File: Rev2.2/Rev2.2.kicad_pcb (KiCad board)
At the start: 4 copper layers, 91.8 x 94.5 mm, 120 parts, among them J1 Termination, J10 USART1, J11 3.3V power breakout, J12 5V power breakout, J13 AIN1, J14 USB C PWR, J15 USART6, J16 AIN2, J17 AIN3, J18 AIN4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

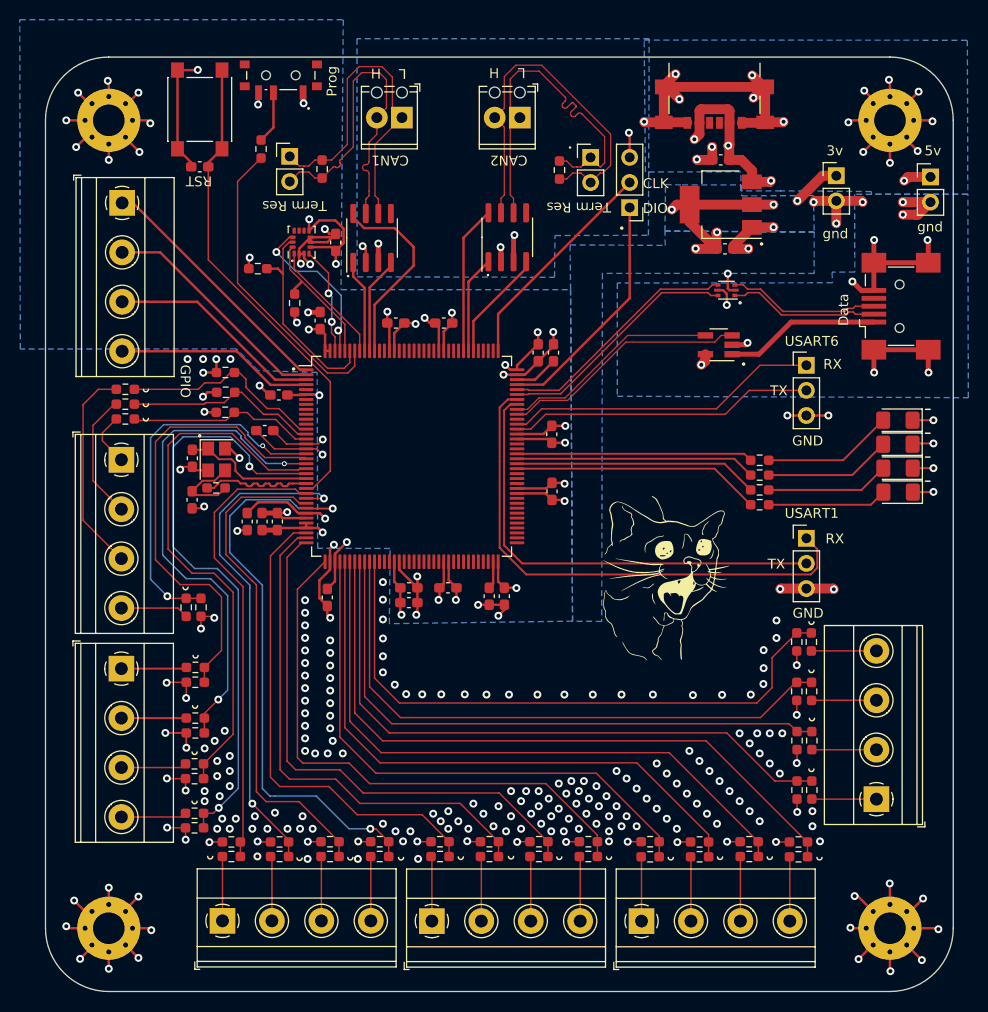
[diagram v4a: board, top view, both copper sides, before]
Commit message: added labels that tell you which pins the connectors are connected to for analog, GPIO, and LEDs. Also added a label for the USB C connector called Power to indicate its function
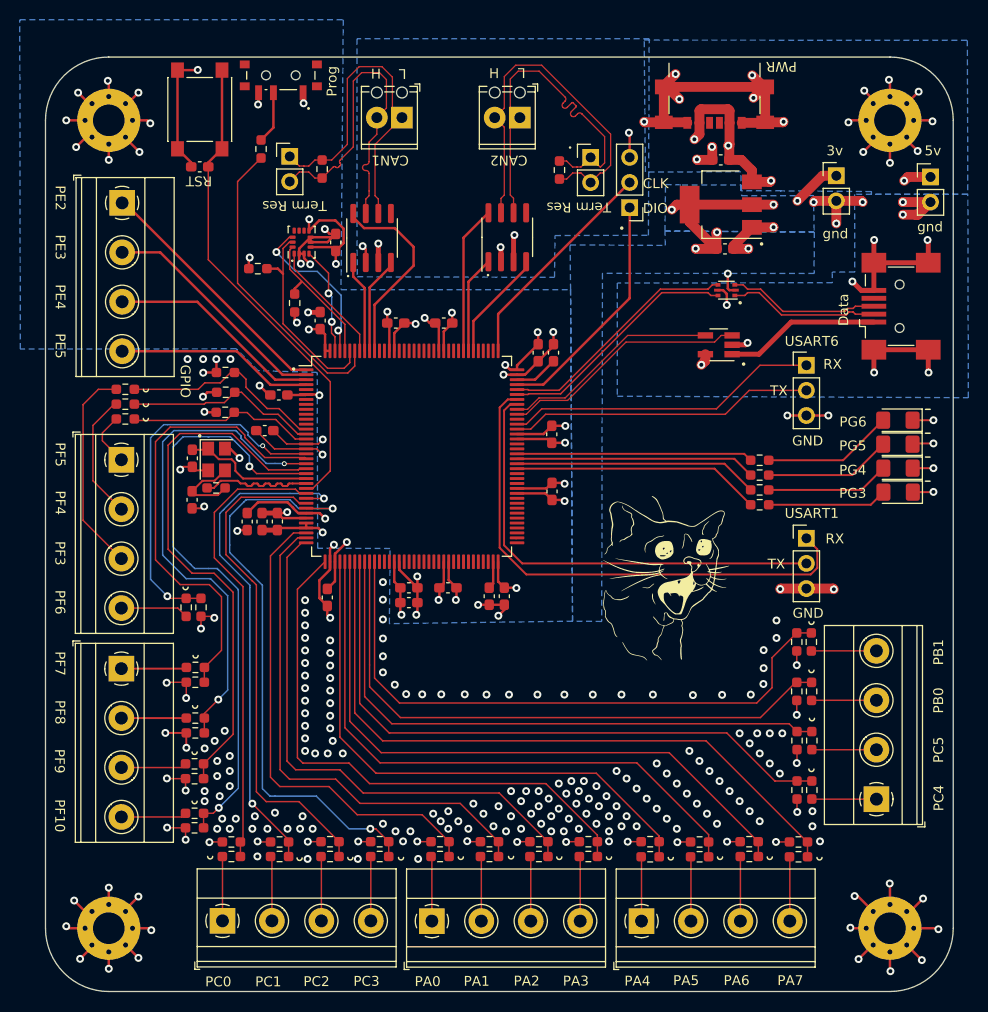
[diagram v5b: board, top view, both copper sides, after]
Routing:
- net GPIO1: track 25.6 -> 26.7 mm
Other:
- board text added: "PA0"
- board text added: "PA1"
- board text added: "PA2"
- board text added: "PA3"
- board text added: "PA4"
- board text added: "PA5"
- board text added: "PA6"
- board text added: "PA7"
- board text added: "PB0"
- board text added: "PB1"
- board text added: "PC0"
- board text added: "PC1"
- board text added: "PC2"
- board text added: "PC3"
- board text added: "PC4"
- board text added: "PC5"
- board text added: "PE2"
- board text added: "PE3"
- board text added: "PE4"
- board text added: "PE5"
- board text added: "PF10"
- board text added: "PF3"
- board text added: "PF4"
- board text added: "PF5"
- board text added: "PF6"
- board text added: "PF7"
- board text added: "PF8"
- board text added: "PF9"
- board text added: "PG3"
- board text added: "PG4"
- board text added: "PG5"
- board text added: "PG6"
- board text added: "PWR"
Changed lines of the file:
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@@
     (effects (font (size 1 1) (thickness 0.15)) (justify left bottom mirror))
   )
+  (gr_text "PC4" (at 191.9224 134.366 90) (layer "F.SilkS")
+    (effects (font (size 1 1) (thickness 0.15)) (justify left bottom))
+  )
   (gr_text "Data\n" (at 182.3 85.3 90) (layer "F.SilkS")
     (effects (font (size 1 1) (thickness 0.15)) (justify left bottom))
   )
+  (gr_text "PWR" (at 176.9872 58.4708 180) (layer "F.SilkS")
+    (effects (font (size 1 1) (thickness 0.15)) (justify left bottom))
+  )
   (gr_text "L\n" (at 137.5 59.2 180) (layer "F.SilkS")
     (effects (font (size 1 1) (thickness 0.15)) (justify left bottom))
@@
     (effects (font (size 1 1) (thickness 0.15)) (justify left bottom))
   )
+  (gr_text "PG6\n" (at 181.2798 95.5802) (layer "F.SilkS")
+    (effects (font (size 1 1) (thickness 0.15)) (justify left bottom))
+  )
+  (gr_text "PC5\n" (at 191.897 129.4892 90) (layer "F.SilkS")
+    (effects (font (size 1 1) (thickness 0.15)) (justify left bottom))
+  )
+  (gr_text "PF5" (at 101.9048 97.0534 270) (layer "F.SilkS")
+    (effects (font (size 1 1) (thickness 0.15)) (justify left bottom))
+  )
   (gr_text "Prog" (at 130.55 62.1 90) (layer "F.SilkS")
     (effects (font (size 1 1) (thickness 0.15)) (justify left bottom))
@@
     (effects (font (size 1 1) (thickness 0.15)) (justify left bottom))
   )
+  (gr_text "PA2" (at 148.336 152.1206) (layer "F.SilkS")
+    (effects (font (size 1 1) (thickness 0.15)) (justify left bottom))
+  )
   (gr_text "3v\n" (at 179.975 68.154) (layer "F.SilkS")
     (effects (font (size 1 1) (thickness 0.15)) (justify left bottom))
   )
+  (gr_text "PG4\n" (at 181.2544 100.457) (layer "F.SilkS")
+    (effects (font (size 1 1) (thickness 0.15)) (justify left bottom))
+  )
+  (gr_text "PA6\n" (at 169.5704 152.0698) (layer "F.SilkS")
+    (effects (font (size 1 1) (thickness 0.15)) (justify left bottom))
+  )
+  (gr_text "PF3" (at 101.8794 107.0356 270) (layer "F.SilkS")
+    (effects (font (size 1 1) (thickness 0.15)) (justify left bottom))
+  )
+  (gr_text "PF9" (at 101.8286 128.0668 270) (layer "F.SilkS")
+    (effects (font (size 1 1) (thickness 0.15)) (justify left bottom))
+  )
+  (gr_text "PA1\n" (at 143.2814 152.146) (layer "F.SilkS")
+    (effects (font (size 1 1) (thickness 0.15)) (justify left bottom))
+  )
   (gr_text "GND\n" (at 176.55 114.925) (layer "F.SilkS")
     (effects (font (size 1 1) (thickness 0.15)) (justify left bottom))
   )
+  (gr_text "PC0" (at 117.1448 152.1968) (layer "F.SilkS")
+    (effects (font (size 1 1) (thickness 0.15)) (justify left bottom))
+  )
+  (gr_text "PE4" (at 101.9048 81.0768 270) (layer "F.SilkS")
+    (effects (font (size 1 1) (thickness 0.15)) (justify left bottom))
+  )
+  (gr_text "PE3" (at 101.9048 76.0476 270) (layer "F.SilkS")
+    (effects (font (size 1 1) (thickness 0.15)) (justify left bottom))
+  )
   (gr_text "5v\n" (at 189.9 68.159) (layer "F.SilkS")
     (effects (font (size 1 1) (thickness 0.15)) (justify left bottom))
@@
     (effects (font (size 1 1) (thickness 0.15)) (justify left bottom))
   )
+  (gr_text "PA7" (at 175.006 152.0698) (layer "F.SilkS")
+    (effects (font (size 1 1) (thickness 0.15)) (justify left bottom))
+  )
+  (gr_text "PA4" (at 159.5374 152.1206) (layer "F.SilkS")
+    (effects (font (size 1 1) (thickness 0.15)) (justify left bottom))
+  )
+  (gr_text "PE2" (at 101.9048 71.0692 270) (layer "F.SilkS")
+    (effects (font (size 1 1) (thickness 0.15)) (justify left bottom))
+  )
   (gr_text "L\n" (at 149.55 59.1 180) (layer "F.SilkS")
     (effects (font (size 1 1) (thickness 0.15)) (justify left bottom))
   )
+  (gr_text "PB0\n" (at 191.897 124.4854 90) (layer "F.SilkS")
+    (effects (font (size 1 1) (thickness 0.15)) (justify left bottom))
+  )
   (gr_text "Term Res" (at 158.2 72.7 180) (layer "F.SilkS")
     (effects (font (size 1 1) (thickness 0.15)) (justify left bottom))
@@
     (effects (font (size 1 1) (thickness 0.15)) (justify left bottom))
   )
+  (gr_text "PF10" (at 101.854 133.1468 -90) (layer "F.SilkS")
+    (effects (font (size 1 1) (thickness 0.15)) (justify left bottom))
+  )
   (gr_text "gnd\n" (at 179.575 76.554) (layer "F.SilkS")
     (effects (font (size 1 1) (thickness 0.15)) (justify left bottom))
@@
     (effects (font (size 1 1) (thickness 0.15)) (justify left bottom))
   )
+  (gr_text "PC3" (at 132.1308 152.146) (layer "F.SilkS")
+    (effects (font (size 1 1) (thickness 0.15)) (justify left bottom))
+  )
   (gr_text "CLK" (at 161.4 71.475) (layer "F.SilkS")
     (effects (font (size 1 1) (thickness 0.15)) (justify left bottom))
   )
+  (gr_text "PE5" (at 101.9048 86.0298 270) (layer "F.SilkS")
+    (effects (font (size 1 1) (thickness 0.15)) (justify left bottom))
+  )
+  (gr_text "PF7" (at 101.8794 118.1862 270) (layer "F.SilkS")
+    (effects (font (size 1 1) (thickness 0.15)) (justify left bottom))
+  )
   (gr_text "GPIO" (at 114.55 89.2 -90) (layer "F.SilkS")
     (effects (font (size 1 1) (thickness 0.15)) (justify left bottom))
@@
     (effects (font (size 1 1) (thickness 0.15)) (justify left bottom))
   )
+  (gr_text "PF8" (at 101.8794 123.1138 270) (layer "F.SilkS")
+    (effects (font (size 1 1) (thickness 0.15)) (justify left bottom))
+  )
   (gr_text "RX" (at 179.65 89.75) (layer "F.SilkS")
     (effects (font (size 1 1) (thickness 0.15)) (justify left bottom))
@@
     (effects (font (size 1 1) (thickness 0.15)) (justify left bottom))
   )
+  (gr_text "PB1" (at 191.897 119.6086 90) (layer "F.SilkS")
+    (effects (font (size 1 1) (thickness 0.15)) (justify left bottom))
+  )
   (gr_text "DIO" (at 161.405 73.99) (layer "F.SilkS")
     (effects (font (size 1 1) (thickness 0.15)) (justify left bottom))
@@
     (effects (font (size 1 1) (thickness 0.15)) (justify left bottom))
   )
+  (gr_text "PC1" (at 122.1994 152.1968) (layer "F.SilkS")
+    (effects (font (size 1 1) (thickness 0.15)) (justify left bottom))
+  )
   (gr_text "TX" (at 174.025 109.95) (layer "F.SilkS")
+    (effects (font (size 1 1) (thickness 0.15)) (justify left bottom))
+  )
+  (gr_text "PG5" (at 181.2544 97.9932) (layer "F.SilkS")
+    (effects (font (size 1 1) (thickness 0.15)) (justify left bottom))
+  )
+  (gr_text "PA3\n" (at 153.3144 152.1206) (layer "F.SilkS")
+    (effects (font (size 1 1) (thickness 0.15)) (justify left bottom))
+  )
+  (gr_text "PF4" (at 101.9048 101.9302 270) (layer "F.SilkS")
+    (effects (font (size 1 1) (thickness 0.15)) (justify left bottom))
+  )
+  (gr_text "PC2" (at 127.0762 152.1714) (layer "F.SilkS")
+    (effects (font (size 1 1) (thickness 0.15)) (justify left bottom))
+  )
+  (gr_text "PA5" (at 164.465 152.0698) (layer "F.SilkS")
+    (effects (font (size 1 1) (thickness 0.15)) (justify left bottom))
+  )
+  (gr_text "PA0" (at 138.3284 152.1714) (layer "F.SilkS")
+    (effects (font (size 1 1) (thickness 0.15)) (justify left bottom))
+  )
+  (gr_text "PG3" (at 181.2544 102.7938) (layer "F.SilkS")
+    (effects (font (size 1 1) (thickness 0.15)) (justify left bottom))
+  )
+  (gr_text "PF6\n" (at 101.8794 111.9886 270) (layer "F.SilkS")
     (effects (font (size 1 1) (thickness 0.15)) (justify left bottom))
   )
@@
   (segment (start 112.6 77.85) (end 124.975 90.225) (width 0.25) (layer "F.Cu") (net 31))
   (segment (start 108.75 72.85) (end 109.85 72.85) (width 0.25) (layer "F.Cu") (net 32))
-  (segment (start 126.725 89.725) (end 127.3625 89.725) (width 0.25) (layer "F.Cu") (net 32))
-  (segment (start 109.85 72.85) (end 126.725 89.725) (width 0.25) (layer "F.Cu") (net 32))
+  (segment (start 109.0196 72.85) (end 125.8946 89.725) (width 0.25) (layer "F.Cu") (net 32))
+  (segment (start 125.8946 89.725) (end 127.3625 89.725) (width 0.25) (layer "F.Cu") (net 32))
+  (segment (start 108.75 72.85) (end 109.0196 72.85) (width 0.25) (layer "F.Cu") (net 32))
   (segment (start 139.9875 138.95) (end 140.075 139.0375) (width 0.15) (layer "F.Cu") (net 33))
   (segment (start 140.075 139.0375) (end 140.075 145.475) (width 0.15) (layer "F.Cu") (net 33))
@@
     )
   )
+  (group "" (id fc9d4f1d-c30f-44bc-aca4-111d54daccf4)
+    (members
+      214925c7-973c-4d41-8aef-7a658da22a7c
+      34d76fdf-a2f4-4277-b68e-b28b638f8da5
+      cdb19b88-fe50-4d2b-b638-e18fe21b3137
+      f81a921d-949b-492d-8175-2068cc33f6d3
+    )
+  )
